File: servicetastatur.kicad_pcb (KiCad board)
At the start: 2 copper layers, 129 x 69 mm, 7 parts, among them U1 AT24CS16-SSHM, U2 TL7705A, U3 74HC165, U4 74HC00, U5 MC34063AP, U6 27C128, Y1 Crystal

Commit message: kleiner
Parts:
- added C1: C_Polarized, Capacitor_THT:CP_Radial_D5.0mm_P2.00mm, F.Cu at (116.0, 107.0)
- added C2: C_Polarized, Capacitor_THT:CP_Radial_D5.0mm_P2.00mm, F.Cu at (116.0, 113.5)
- added J1: Conn_01x16_Socket, Connector_JST:JST_ZE_B16B-ZESK-1D_1x16_P1.50mm_Vertical, F.Cu at (96.5, 134.0)
- added J2: Conn_01x06_Socket, Connector_Hirose:Hirose_DF63-6P-3.96DSA_1x06_P3.96mm_Vertical, F.Cu at (141.2, 89.0)
- moved U5 5.86 mm to (147.4, 134.0)
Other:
- board size 129 x 69 mm -> 122 x 61 mm

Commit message: war nochmal kleiner
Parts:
- moved U5 11.2 mm to (147.2, 122.8)
- moved J1 7.02 mm to (97.0, 127.0)
- moved U2 5.74 mm to (160.5, 84.0)
- moved J2 5.18 mm to (136.1, 88.0)
- moved U4 5.00 mm to (86.4, 97.8)
- moved U1 4.82 mm to (122.4, 83.8)
- moved C1 3.41 mm to (118.9, 105.2)
- moved U6 3.41 mm to (82.1, 120.2)
- moved C2 3.41 mm to (118.9, 111.8)
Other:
- board size 122 x 61 mm -> 100 x 55 mm
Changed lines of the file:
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@@
   )
   (footprint "Package_DIP:DIP-8_W7.62mm" (layer "F.Cu")
-    (at 147.38 134 90)
+    (at 147.2 122.8 90)
     (descr "8-lead though-hole mounted DIP package, row spacing 7.62 mm (300 mils)")
     (tags "THT DIP DIL PDIP 2.54mm 7.62mm 300mil")
@@
   )
   (footprint "Connector_Hirose:Hirose_DF63-6P-3.96DSA_1x06_P3.96mm_Vertical" (layer "F.Cu")
-    (at 141.16 89)
+    (at 136.08 88)
     (descr "Hirose DF63 through hole, DF63-6P-3.96DSA, 6 Pins per row (https://www.hirose.com/product/en/products/DF63/), generated with kicad-footprint-generator")
     (tags "connector Hirose DF63 vertical")
@@
   )
   (footprint "Package_DIP:DIP-28_W15.24mm" (layer "F.Cu")
-    (at 79.14 122 90)
+    (at 82.06 120.24 90)
     (descr "28-lead though-hole mounted DIP package, row spacing 15.24 mm (600 mils)")
     (tags "THT DIP DIL PDIP 2.54mm 15.24mm 600mil")
@@
   )
   (footprint "Connector_JST:JST_ZE_B16B-ZESK-1D_1x16_P1.50mm_Vertical" (layer "F.Cu")
-    (at 96.5 134)
+    (at 97 127)
     (descr "JST ZE series connector, B16B-ZESK-1D, with boss (http://www.jst-mfg.com/product/pdf/eng/eZE.pdf), generated with kicad-footprint-generator")
     (tags "connector JST ZE side entry boss")
@@
   )
   (footprint "Capacitor_THT:CP_Radial_D5.0mm_P2.00mm" (layer "F.Cu")
-    (at 116 113.55)
+    (at 118.92 111.79)
     (descr "CP, Radial series, Radial, pin pitch=2.00mm, , diameter=5mm, Electrolytic Capacitor")
     (tags "CP Radial series Radial pin pitch 2.00mm  diameter 5mm Electrolytic Capacitor")
@@
   )
   (footprint "Package_DIP:DIP-8_W7.62mm" (layer "F.Cu")
-    (at 127.2 83.8 90)
+    (at 122.38 83.8 90)
     (descr "8-lead though-hole mounted DIP package, row spacing 7.62 mm (300 mils)")
     (tags "THT DIP DIL PDIP 2.54mm 7.62mm 300mil")
@@
   )
   (footprint "Package_DIP:DIP-14_W7.62mm" (layer "F.Cu")
-    (at 82.375 100.8 90)
+    (at 86.375 97.8 90)
     (descr "14-lead though-hole mounted DIP package, row spacing 7.62 mm (300 mils)")
     (tags "THT DIP DIL PDIP 2.54mm 7.62mm 300mil")
@@
   )
   (footprint "Capacitor_THT:CP_Radial_D5.0mm_P2.00mm" (layer "F.Cu")
-    (at 116 107)
+    (at 118.92 105.24)
     (descr "CP, Radial series, Radial, pin pitch=2.00mm, , diameter=5mm, Electrolytic Capacitor")
     (tags "CP Radial series Radial pin pitch 2.00mm  diameter 5mm Electrolytic Capacitor")
@@
   )
   (footprint "Package_DIP:DIP-8_W7.62mm" (layer "F.Cu")
-    (at 166.2 84 90)
+    (at 160.46 84 90)
     (descr "8-lead though-hole mounted DIP package, row spacing 7.62 mm (300 mils)")
     (tags "THT DIP DIL PDIP 2.54mm 7.62mm 300mil")
@@
     )
   )
-  (gr_line (start 85 136) (end 194 136)
+  (gr_line (start 85 130) (end 174 130)
     (stroke (width 0.1) (type default)) (layer "Edge.Cuts"))
-  (gr_line (start 194 75) (end 86 75)
+  (gr_line (start 175 75) (end 86 75)
     (stroke (width 0.1) (type default)) (layer "Edge.Cuts"))
-  (gr_line (start 85 130) (end 85 136)
+  (gr_line (start 85 130) (end 85 124)
     (stroke (width 0.1) (type default)) (layer "Edge.Cuts"))
-  (gr_line (start 78 84) (end 78 130)
+  (gr_line (start 80 80) (end 80 124)
     (stroke (width 0.1) (type default)) (layer "Edge.Cuts"))
-  (gr_line (start 78 130) (end 85 130)
+  (gr_line (start 80 124) (end 85 124)
     (stroke (width 0.1) (type default)) (layer "Edge.Cuts"))
-  (gr_line (start 194 136) (end 194 130)
+  (gr_line (start 174 130) (end 174 124)
     (stroke (width 0.1) (type default)) (layer "Edge.Cuts"))
-  (gr_line (start 194 130) (end 200 130)
+  (gr_line (start 174 124) (end 180 124)
     (stroke (width 0.1) (type default)) (layer "Edge.Cuts"))
-  (gr_line (start 194 84) (end 194 75)
+  (gr_line (start 175 80) (end 175 75)
     (stroke (width 0.1) (type default)) (layer "Edge.Cuts"))
-  (gr_line (start 86 84) (end 78 84)
+  (gr_line (start 86 80) (end 80 80)
     (stroke (width 0.1) (type default)) (layer "Edge.Cuts"))
-  (gr_line (start 200 84) (end 194 84)
+  (gr_line (start 180 80) (end 175 80)
     (stroke (width 0.1) (type default)) (layer "Edge.Cuts"))
-  (gr_line (start 86 75) (end 86 84)
+  (gr_line (start 86 75) (end 86 80)
     (stroke (width 0.1) (type default)) (layer "Edge.Cuts"))
-  (gr_line (start 200 130) (end 200 84)
+  (gr_line (start 180 124) (end 180 80)
     (stroke (width 0.1) (type default)) (layer "Edge.Cuts"))
 )

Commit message: wieder groesser
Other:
- board size 100 x 55 mm -> 100 x 60 mm
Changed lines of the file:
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@@
     )
   )
-  (gr_line (start 85 130) (end 174 130)
+  (gr_line (start 85 135) (end 174 135)
     (stroke (width 0.1) (type default)) (layer "Edge.Cuts"))
   (gr_line (start 175 75) (end 86 75)
     (stroke (width 0.1) (type default)) (layer "Edge.Cuts"))
-  (gr_line (start 85 130) (end 85 124)
+  (gr_line (start 85 135) (end 85 129)
     (stroke (width 0.1) (type default)) (layer "Edge.Cuts"))
-  (gr_line (start 80 80) (end 80 124)
+  (gr_line (start 80 80) (end 80 129)
     (stroke (width 0.1) (type default)) (layer "Edge.Cuts"))
-  (gr_line (start 80 124) (end 85 124)
+  (gr_line (start 80 129) (end 85 129)
     (stroke (width 0.1) (type default)) (layer "Edge.Cuts"))
-  (gr_line (start 174 130) (end 174 124)
+  (gr_line (start 174 135) (end 174 129)
     (stroke (width 0.1) (type default)) (layer "Edge.Cuts"))
-  (gr_line (start 174 124) (end 180 124)
+  (gr_line (start 174 129) (end 180 129)
     (stroke (width 0.1) (type default)) (layer "Edge.Cuts"))
   (gr_line (start 175 80) (end 175 75)
@@
   (gr_line (start 86 75) (end 86 80)
     (stroke (width 0.1) (type default)) (layer "Edge.Cuts"))
-  (gr_line (start 180 124) (end 180 80)
+  (gr_line (start 180 129) (end 180 80)
     (stroke (width 0.1) (type default)) (layer "Edge.Cuts"))
 )

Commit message: groesse
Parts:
- moved U1 6.82 mm to (129.2, 83.8)
- moved J1 4.92 mm to (101.5, 129.0)
- moved J2 2.27 mm to (137.2, 90.0)
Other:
- board size 100 x 60 mm -> 106 x 57 mm
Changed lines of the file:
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@@
   )
   (footprint "Connector_Hirose:Hirose_DF63-6P-3.96DSA_1x06_P3.96mm_Vertical" (layer "F.Cu")
-    (at 136.08 88)
+    (at 137.16 90)
     (descr "Hirose DF63 through hole, DF63-6P-3.96DSA, 6 Pins per row (https://www.hirose.com/product/en/products/DF63/), generated with kicad-footprint-generator")
     (tags "connector Hirose DF63 vertical")
@@
   )
   (footprint "Connector_JST:JST_ZE_B16B-ZESK-1D_1x16_P1.50mm_Vertical" (layer "F.Cu")
-    (at 97 127)
+    (at 101.5 129)
     (descr "JST ZE series connector, B16B-ZESK-1D, with boss (http://www.jst-mfg.com/product/pdf/eng/eZE.pdf), generated with kicad-footprint-generator")
     (tags "connector JST ZE side entry boss")
@@
   )
   (footprint "Package_DIP:DIP-8_W7.62mm" (layer "F.Cu")
-    (at 122.38 83.8 90)
+    (at 129.2 83.8 90)
     (descr "8-lead though-hole mounted DIP package, row spacing 7.62 mm (300 mils)")
     (tags "THT DIP DIL PDIP 2.54mm 7.62mm 300mil")
@@
     )
   )
-  (gr_line (start 85 135) (end 174 135)
+  (gr_line (start 88 132) (end 175 132)
     (stroke (width 0.1) (type default)) (layer "Edge.Cuts"))
-  (gr_line (start 175 75) (end 86 75)
+  (gr_line (start 175 75) (end 88 75)
     (stroke (width 0.1) (type default)) (layer "Edge.Cuts"))
-  (gr_line (start 85 135) (end 85 129)
+  (gr_line (start 88 132) (end 88 124)
     (stroke (width 0.1) (type default)) (layer "Edge.Cuts"))
-  (gr_line (start 80 80) (end 80 129)
+  (gr_line (start 80 83) (end 80 124)
     (stroke (width 0.1) (type default)) (layer "Edge.Cuts"))
-  (gr_line (start 80 129) (end 85 129)
+  (gr_line (start 80 124) (end 88 124)
     (stroke (width 0.1) (type default)) (layer "Edge.Cuts"))
-  (gr_line (start 174 135) (end 174 129)
+  (gr_line (start 175 132) (end 175 123)
     (stroke (width 0.1) (type default)) (layer "Edge.Cuts"))
-  (gr_line (start 174 129) (end 180 129)
+  (gr_line (start 175 123) (end 186 123)
     (stroke (width 0.1) (type default)) (layer "Edge.Cuts"))
-  (gr_line (start 175 80) (end 175 75)
+  (gr_line (start 175 84) (end 175 75)
     (stroke (width 0.1) (type default)) (layer "Edge.Cuts"))
-  (gr_line (start 86 80) (end 80 80)
+  (gr_line (start 88 83) (end 80 83)
     (stroke (width 0.1) (type default)) (layer "Edge.Cuts"))
-  (gr_line (start 180 80) (end 175 80)
+  (gr_line (start 186 84) (end 175 84)
     (stroke (width 0.1) (type default)) (layer "Edge.Cuts"))
-  (gr_line (start 86 75) (end 86 80)
+  (gr_line (start 88 75) (end 88 83)
     (stroke (width 0.1) (type default)) (layer "Edge.Cuts"))
-  (gr_line (start 180 129) (end 180 80)
+  (gr_line (start 186 123) (end 186 84)
     (stroke (width 0.1) (type default)) (layer "Edge.Cuts"))
 )

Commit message: rumgeschiebe
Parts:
- J2: footprint Connector_Hirose:Hirose_DF63-6P-3.96DSA_1x06_P3.96mm_Vertical -> Connector_JST:JST_PH_S6B-PH-K_1x06_P2.00mm_Horizontal
- moved U5 10.6 mm to (139.2, 129.8)
- moved J2 5.16 mm to (141.0, 86.5)
- moved J1 5.10 mm to (96.5, 130.0)
- moved U1 4.12 mm to (125.2, 84.8)
- moved U3 4.00 mm to (126.3, 105.0)
- moved U2 3.26 mm to (157.2, 84.0)
- moved U4 3.16 mm to (83.4, 98.8)
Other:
- outline, holes or cut-outs redrawn

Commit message: anschluss
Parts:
- J1: footprint Connector_JST:JST_ZE_B16B-ZESK-1D_1x16_P1.50mm_Vertical -> Connector_Molex:Molex_Picoflex_90325-0016_2x08_P1.27mm_Vertical
- J2: footprint Connector_JST:JST_PH_S6B-PH-K_1x06_P2.00mm_Horizontal -> Connector_Molex:Molex_SPOX_5268-06A_1x06_P2.50mm_Horizontal
- moved J1 4.91 mm to (101.2, 128.5), turned to 90 degrees
- moved J2 2.26 mm to (138.8, 86.3)
- moved U5 2.20 mm to (137.0, 129.8)
- moved U3 1.84 mm to (124.5, 105.0)
- moved U4 0.55 mm to (83.9, 98.8)
- moved U6 0.40 mm to (82.5, 120.2)
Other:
- outline, holes or cut-outs redrawn

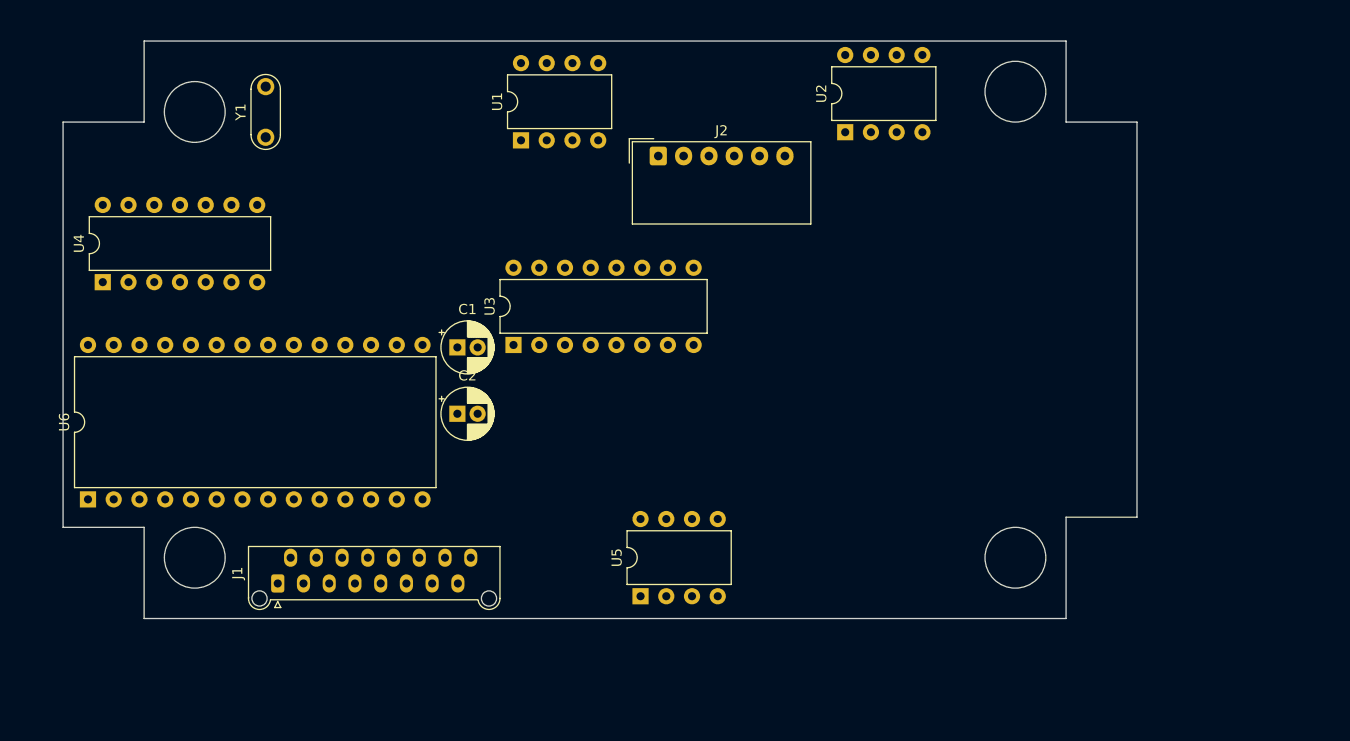
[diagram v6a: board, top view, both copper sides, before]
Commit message: elkos gedreht
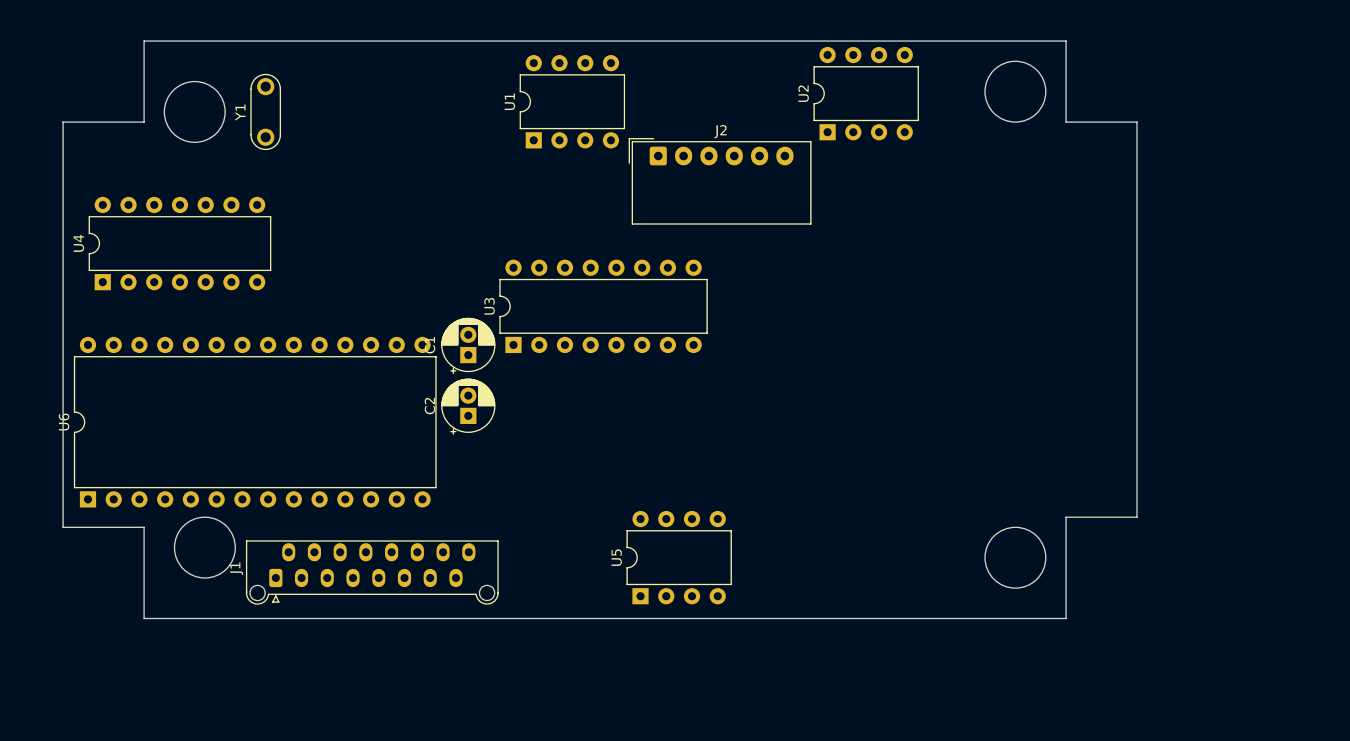
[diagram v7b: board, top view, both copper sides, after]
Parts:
- moved U2 1.74 mm to (155.5, 84.0)
- moved C1 1.32 mm to (120.0, 106.0), turned to 90 degrees
- moved U1 1.26 mm to (126.5, 84.8)
- moved C2 1.10 mm to (120.0, 112.0), turned to 90 degrees
- moved J1 0.57 mm to (101.0, 128.0)
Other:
- outline, holes or cut-outs redrawn
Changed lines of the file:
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@@
   )
   (footprint "Connector_Molex:Molex_Picoflex_90325-0016_2x08_P1.27mm_Vertical" (layer "F.Cu")
-    (at 101.19 128.54 90)
+    (at 101 128 90)
     (descr "Molex Picoflex Ribbon-Cable Connectors, 90325-0016, 16 Pins (http://www.molex.com/pdm_docs/sd/903250004_sd.pdf), generated with kicad-footprint-generator")
     (tags "connector Molex Picoflex side entry")
@@
   )
   (footprint "Capacitor_THT:CP_Radial_D5.0mm_P2.00mm" (layer "F.Cu")
-    (at 118.92 111.79)
+    (at 120 112 90)
     (descr "CP, Radial series, Radial, pin pitch=2.00mm, , diameter=5mm, Electrolytic Capacitor")
     (tags "CP Radial series Radial pin pitch 2.00mm  diameter 5mm Electrolytic Capacitor")
@@
     (property "ki_keywords" "cap capacitor")
     (attr through_hole)
-    (fp_text reference "C2" (at 1 -3.75) (layer "F.SilkS")
-        (effects (font (size 1 1) (thickness 0.15)))
-    )
-    (fp_text value "C_Polarized" (at 1 3.75) (layer "F.Fab")
-        (effects (font (size 1 1) (thickness 0.15)))
-    )
-    (fp_text user "${REFERENCE}" (at 1 0) (layer "F.Fab")
+    (fp_text reference "C2" (at 1 -3.75 90) (layer "F.SilkS")
+        (effects (font (size 1 1) (thickness 0.15)))
+    )
+    (fp_text value "C_Polarized" (at 1 3.75 90) (layer "F.Fab")
+        (effects (font (size 1 1) (thickness 0.15)))
+    )
+    (fp_text user "${REFERENCE}" (at 1 0 90) (layer "F.Fab")
         (effects (font (size 1 1) (thickness 0.15)))
     )
@@
     (fp_circle (center 1 0) (end 3.5 0)
       (stroke (width 0.1) (type solid)) (fill none) (layer "F.Fab"))
-    (pad "1" thru_hole rect (at 0 0) (size 1.6 1.6) (drill 0.8) (layers "*.Cu" "*.Mask")
+    (pad "1" thru_hole rect (at 0 0 90) (size 1.6 1.6) (drill 0.8) (layers "*.Cu" "*.Mask")
       (net 87 "unconnected-(C2-Pad1)") (pintype "passive"))
-    (pad "2" thru_hole circle (at 2 0) (size 1.6 1.6) (drill 0.8) (layers "*.Cu" "*.Mask")
+    (pad "2" thru_hole circle (at 2 0 90) (size 1.6 1.6) (drill 0.8) (layers "*.Cu" "*.Mask")
       (net 88 "unconnected-(C2-Pad2)") (pintype "passive"))
     (model "${KICAD6_3DMODEL_DIR}/Capacitor_THT.3dshapes/CP_Radial_D5.0mm_P2.00mm.wrl"
@@
   )
   (footprint "Package_DIP:DIP-8_W7.62mm" (layer "F.Cu")
-    (at 125.2 84.8 90)
+    (at 126.46 84.8 90)
     (descr "8-lead though-hole mounted DIP package, row spacing 7.62 mm (300 mils)")
     (tags "THT DIP DIL PDIP 2.54mm 7.62mm 300mil")
@@
   )
   (footprint "Capacitor_THT:CP_Radial_D5.0mm_P2.00mm" (layer "F.Cu")
-    (at 118.92 105.24)
+    (at 120 106 90)
     (descr "CP, Radial series, Radial, pin pitch=2.00mm, , diameter=5mm, Electrolytic Capacitor")
     (tags "CP Radial series Radial pin pitch 2.00mm  diameter 5mm Electrolytic Capacitor")
@@
     (property "ki_keywords" "cap capacitor")
     (attr through_hole)
-    (fp_text reference "C1" (at 1 -3.75) (layer "F.SilkS")
-        (effects (font (size 1 1) (thickness 0.15)))
-    )
-    (fp_text value "C_Polarized" (at 1 3.75) (layer "F.Fab")
-        (effects (font (size 1 1) (thickness 0.15)))
-    )
-    (fp_text user "${REFERENCE}" (at 1 0) (layer "F.Fab")
+    (fp_text reference "C1" (at 1 -3.75 90) (layer "F.SilkS")
+        (effects (font (size 1 1) (thickness 0.15)))
+    )
+    (fp_text value "C_Polarized" (at 1 3.75 90) (layer "F.Fab")
+        (effects (font (size 1 1) (thickness 0.15)))
+    )
+    (fp_text user "${REFERENCE}" (at 1 0 90) (layer "F.Fab")
         (effects (font (size 1 1) (thickness 0.15)))
     )
@@
     (fp_circle (center 1 0) (end 3.5 0)
       (stroke (width 0.1) (type solid)) (fill none) (layer "F.Fab"))
-    (pad "1" thru_hole rect (at 0 0) (size 1.6 1.6) (drill 0.8) (layers "*.Cu" "*.Mask")
+    (pad "1" thru_hole rect (at 0 0 90) (size 1.6 1.6) (drill 0.8) (layers "*.Cu" "*.Mask")
       (net 85 "unconnected-(C1-Pad1)") (pintype "passive"))
-    (pad "2" thru_hole circle (at 2 0) (size 1.6 1.6) (drill 0.8) (layers "*.Cu" "*.Mask")
+    (pad "2" thru_hole circle (at 2 0 90) (size 1.6 1.6) (drill 0.8) (layers "*.Cu" "*.Mask")
       (net 86 "unconnected-(C1-Pad2)") (pintype "passive"))
     (model "${KICAD6_3DMODEL_DIR}/Capacitor_THT.3dshapes/CP_Radial_D5.0mm_P2.00mm.wrl"
@@
   )
   (footprint "Package_DIP:DIP-8_W7.62mm" (layer "F.Cu")
-    (at 157.2 84 90)
+    (at 155.46 84 90)
     (descr "8-lead though-hole mounted DIP package, row spacing 7.62 mm (300 mils)")
     (tags "THT DIP DIL PDIP 2.54mm 7.62mm 300mil")
@@
   (gr_circle (center 174 80) (end 174 77)
     (stroke (width 0.1) (type default)) (fill none) (layer "Edge.Cuts"))
-  (gr_circle (center 93 126) (end 93 123)
+  (gr_circle (center 94 125) (end 94 122)
     (stroke (width 0.1) (type default)) (fill none) (layer "Edge.Cuts"))
   (gr_line (start 88 132) (end 179 132)

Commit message: i mag ned mehr
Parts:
- J2: footprint Connector_Molex:Molex_SPOX_5268-06A_1x06_P2.50mm_Horizontal -> Connector_Molex:Molex_Nano-Fit_105313-xx06_1x06_P2.50mm_Horizontal
- moved J2 12.3 mm to (151.0, 85.0), turned to -90 degrees
- moved J1 1.54 mm to (99.5, 128.0)
- moved U2 1.00 mm to (155.5, 85.0)
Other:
- outline, holes or cut-outs redrawn
